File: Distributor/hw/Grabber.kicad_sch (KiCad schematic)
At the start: 13 parts, among them J1 Conn_01x04, J2 Conn_01x06_MountingPin, J3 Conn_02x09_Odd_Even, U2 STM32G070CBTx

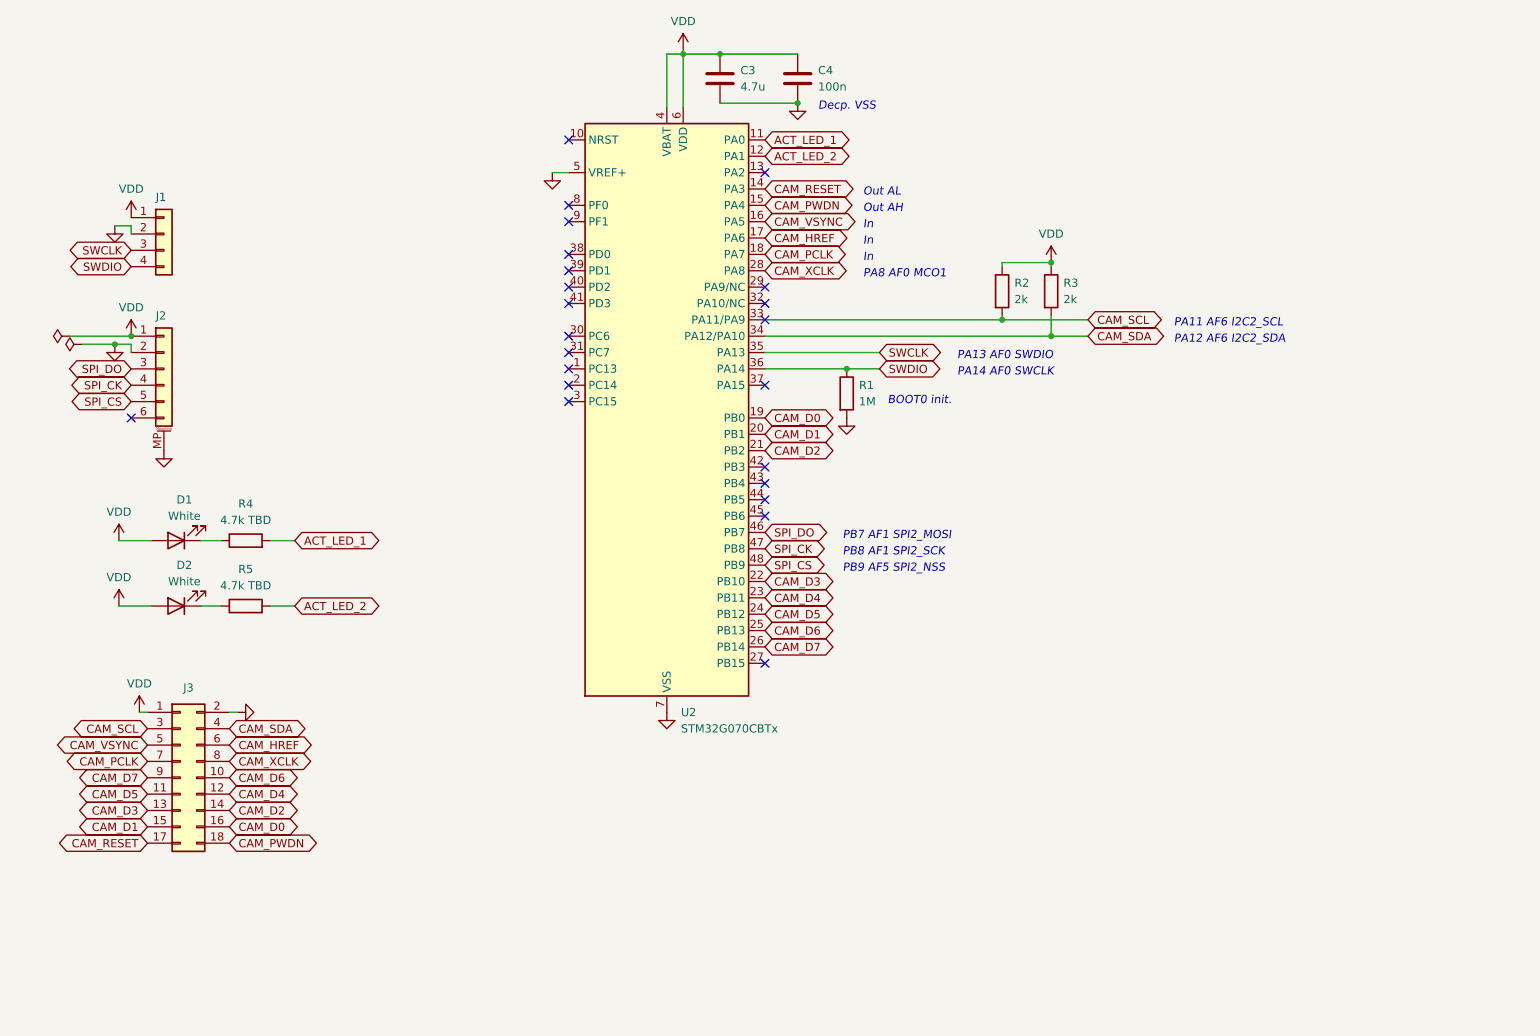
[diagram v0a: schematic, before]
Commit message: Merge distributor and grabber schematic into one
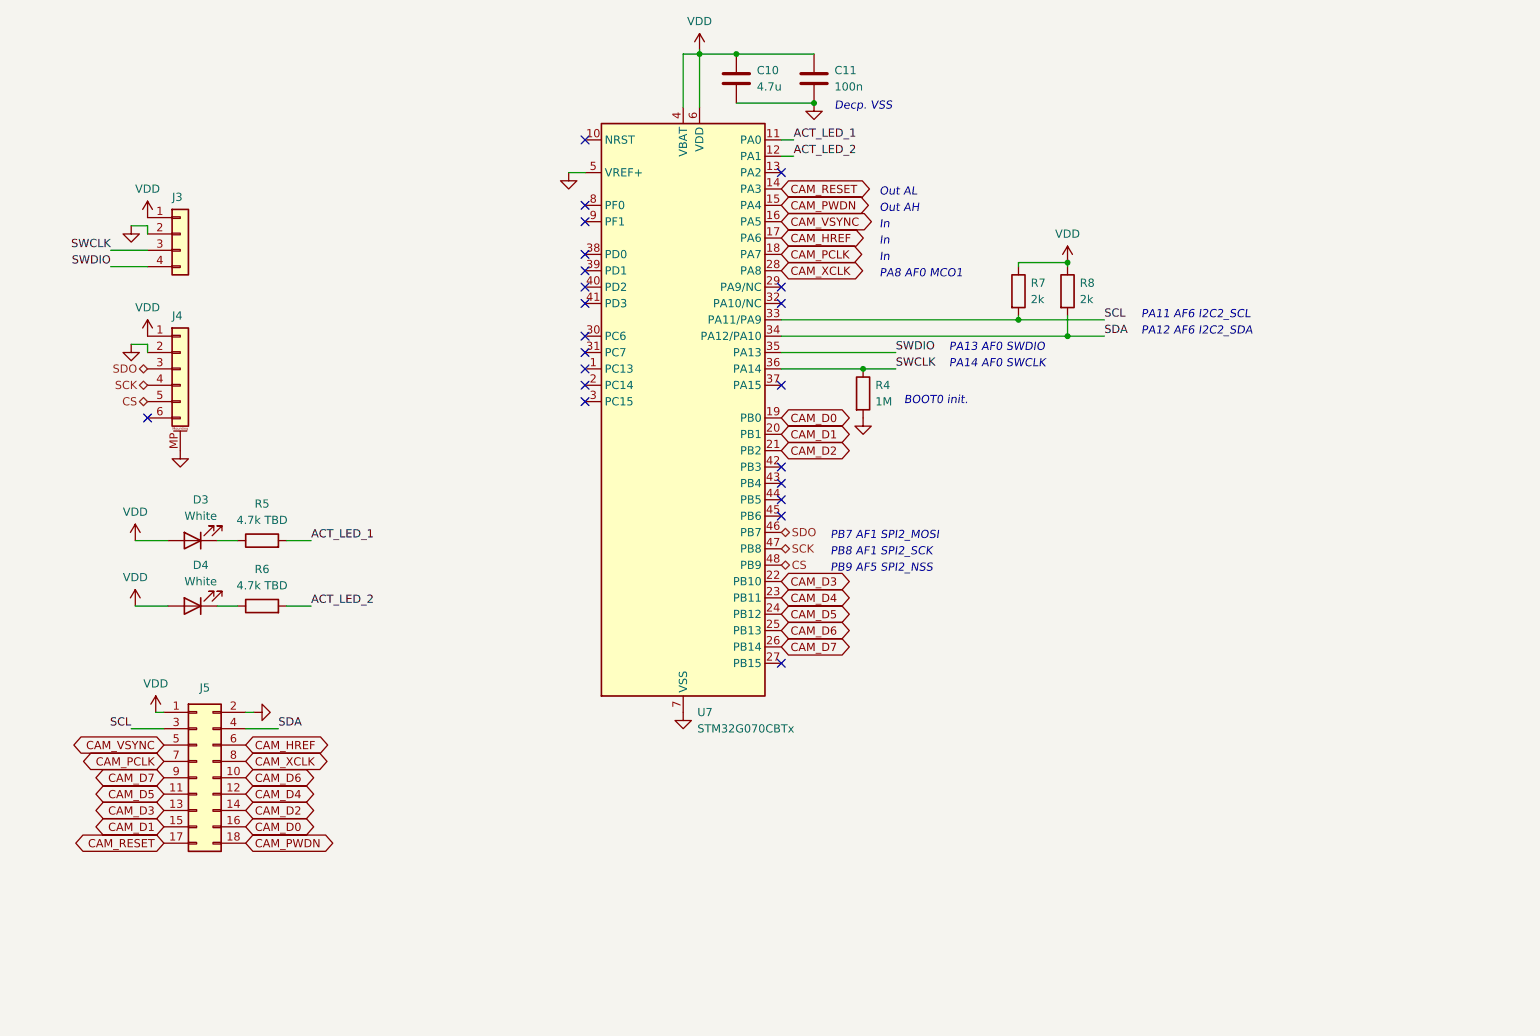
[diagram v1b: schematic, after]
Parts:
- removed C3: 4.7u, Capacitor_SMD:C_0603_1608Metric, symbol Device:C
- removed C4: 100n, Capacitor_SMD:C_0603_1608Metric, symbol Device:C
- removed D1, D2: White, LED_SMD:LED_0603_1608Metric, symbol Device:LED
- removed J1: Conn_01x04, Grabber_footprints:TestPoints_1x04_P2.0, symbol Connector_Generic:Conn_01x04
- removed J2: Conn_01x06_MountingPin, Connector_FFC-FPC:TE_84952-6_1x06-1MP_P1.0mm_Horizontal, symbol Connector_Generic_MountingPin:Conn_01x06_MountingPin
- removed J3: Conn_02x09_Odd_Even, Connector_PinHeader_2.54mm:PinHeader_2x09_P2.54mm_Vertical, symbol Connector_Generic:Conn_02x09_Odd_Even
- removed R1: 1M, Resistor_SMD:R_0603_1608Metric, symbol Device:R
- removed R2, R3: 2k, Resistor_SMD:R_0603_1608Metric, symbol Device:R
- removed U2: STM32G070CBTx, Package_QFP:LQFP-48_7x7mm_P0.5mm, symbol MCU_ST_STM32G0:STM32G070CBTx
- added C10: 4.7u, Capacitor_SMD:C_0603_1608Metric, symbol Device:C
- added C11: 100n, Capacitor_SMD:C_0603_1608Metric, symbol Device:C
- added D3, D4: White, LED_SMD:LED_0603_1608Metric, symbol Device:LED
- added J3: Conn_01x04, Distributor_footprints:TestPoints_1x04_P2.0, symbol Connector_Generic:Conn_01x04
- added J4: Conn_01x06_MountingPin, Connector_FFC-FPC:TE_84952-6_1x06-1MP_P1.0mm_Horizontal, symbol Connector_Generic_MountingPin:Conn_01x06_MountingPin
- added J5: Conn_02x09_Odd_Even, Connector_PinHeader_2.54mm:PinHeader_2x09_P2.54mm_Vertical, symbol Connector_Generic:Conn_02x09_Odd_Even
- added R6: 4.7k TBD, Resistor_SMD:R_0603_1608Metric, symbol Device:R
- added R7, R8: 2k, Resistor_SMD:R_0603_1608Metric, symbol Device:R
- added U7: STM32G070CBTx, Package_QFP:LQFP-48_7x7mm_P0.5mm, symbol MCU_ST_STM32G0:STM32G070CBTx
- R4: value 4.7k TBD -> 1M
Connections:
- net ACT_LED_1: now also R5.2, U7.11 (PA0); no longer R4.2
- net ACT_LED_2: now also R6.2, U7.12 (PA1); no longer R5.2
- net CAM_D0: now also J5.16 (Pin_16), U7.19 (PB0)
- net CAM_D1: now also J5.15 (Pin_15), U7.20 (PB1)
- net CAM_D2: now also J5.14 (Pin_14), U7.21 (PB2)
- net CAM_D3: now also J5.13 (Pin_13), U7.22 (PB10)
- net CAM_D4: now also J5.12 (Pin_12), U7.23 (PB11)
- net CAM_D5: now also J5.11 (Pin_11), U7.24 (PB12)
- net CAM_D6: now also J5.10 (Pin_10), U7.25 (PB13)
- net CAM_D7: now also J5.9 (Pin_9), U7.26 (PB14)
- net CAM_HREF: now also J5.6 (Pin_6), U7.17 (PA6)
- net CAM_PCLK: now also J5.7 (Pin_7), U7.18 (PA7)
- net CAM_PWDN: now also J5.18 (Pin_18), U7.15 (PA4)
- net CAM_RESET: now also J5.17 (Pin_17), U7.14 (PA3)
- net CAM_VSYNC: now also J5.5 (Pin_5), U7.16 (PA5)
- net CAM_XCLK: now also J5.8 (Pin_8), U7.28 (PA8)
- net GND: now also R4.2, C10.2, C11.2, J3.2 (Pin_2), J4.2 (Pin_2), J4.MP (MountPin), J5.2 (Pin_2), U7.5 (VREF+), U7.7 (VSS)
- net SWCLK: now also R4.1, J3.3 (Pin_3), U7.36 (PA14)
- net SWDIO: now also J3.4 (Pin_4), U7.35 (PA13)
- net VDD: now also C10.1, C11.1, D3.2 (A), D4.2 (A), J3.1 (Pin_1), J4.1 (Pin_1), J5.1 (Pin_1), R7.1, R8.1, U7.4 (VBAT), U7.6 (VDD)
- net at R5.1: now also D3.1 (K)
- new net: D4.1 (K), R6.1
- new net CS: J4.5 (Pin_5), U7.48 (PB9)
- new net SCK: J4.4 (Pin_4), U7.47 (PB8)
- new net SCL: J5.3 (Pin_3), R7.2, U7.33 (PA11/PA9)
- new net SDA: J5.4 (Pin_4), R8.2, U7.34 (PA12/PA10)
- new net SDO: J4.3 (Pin_3), U7.46 (PB7)
- no-connect marks 23 -> 22

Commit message: Add MLX90640 sensor to schematic
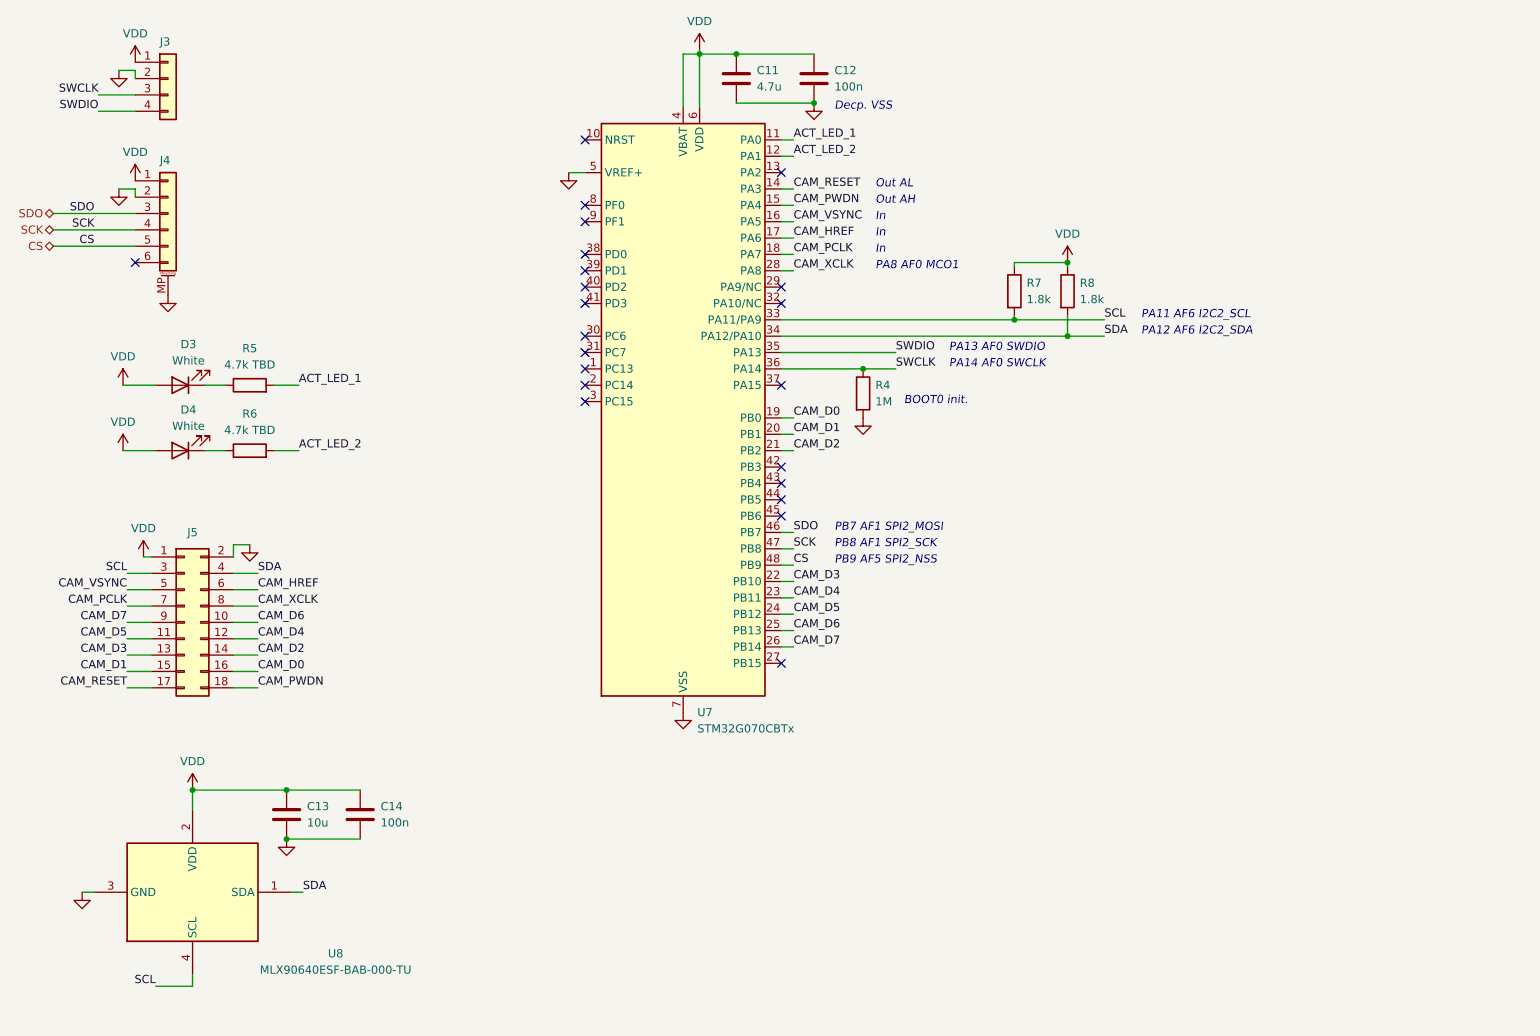
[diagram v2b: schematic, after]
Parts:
- added C13: 10u, Capacitor_SMD:C_0603_1608Metric, symbol Device:C
- added C14: 100n, Capacitor_SMD:C_0603_1608Metric, symbol Device:C
- added U8: MLX90640ESF-BAB-000-TU, MLX90640ESF-BAB-000-TU:MLX90640ESFBAB000TU, symbol MLX90640ESF-BAB-000-TU:MLX90640ESF-BAB-000-TU
- J4: footprint Connector_FFC-FPC:TE_84952-6_1x06-1MP_P1.0mm_Horizontal -> Connector_FFC-FPC:Jushuo_AFC07-S06FCA-00_1x6-1MP_P0.50_Horizontal
- R7, R8: value 2k -> 1.8k
- renumbered C10 to C11, C11 to C12
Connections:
- net GND: now also C13.2, C14.2, U8.3 (GND)
- net SCL: now also U8.4 (SCL)
- net SDA: now also U8.1 (SDA)
- net VDD: now also C13.1, C14.1, U8.2 (VDD)
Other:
- moved on the sheet: D3, D4, J3, J4, J5, R5, R6, R7

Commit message: Separate 5V power supplies into four domains
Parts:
- renumbered C11 to C13, C12 to C14, C13 to C15, C14 to C16, J3 to J7, J4 to J8, J5 to J9

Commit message: Board layout
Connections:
- net GND: no longer U7.5 (VREF+)
- net VDD: now also U7.5 (VREF+)
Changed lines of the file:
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@@
     (stroke (width 0) (type default))
   )
-  (wire (pts (xy 103.505 43.18) (xy 106.045 43.18))
+  (wire (pts (xy 102.235 43.18) (xy 106.045 43.18))
     (stroke (width 0) (type default))
   )
@@
         (path "/3f67d80a-1b5b-4b57-a63e-46eb7de4787a/d071538b-874a-4835-97d2-570c76260972"
           (reference "#PWR043") (unit 1)
-        )
-      )
-    )
-  )
-  (symbol (lib_id "power:GND") (at 103.505 43.18 0) (unit 1)
-    (in_bom yes) (on_board yes) (dnp no) (fields_autoplaced)
-    (property "Reference" "#PWR049" (at 103.505 49.53 0)
-      (effects (font (size 1.27 1.27)) hide)
-    )
-    (property "Value" "GND" (at 103.505 47.625 0)
-      (effects (font (size 1.27 1.27)) hide)
-    )
-    (property "Footprint" "" (at 103.505 43.18 0)
-      (effects (font (size 1.27 1.27)) hide)
-    )
-    (property "Datasheet" "" (at 103.505 43.18 0)
-      (effects (font (size 1.27 1.27)) hide)
-    )
-    (pin "1")
-    (instances
-      (project "Distributor"
-        (path "/3f67d80a-1b5b-4b57-a63e-46eb7de4787a/d071538b-874a-4835-97d2-570c76260972"
-          (reference "#PWR049") (unit 1)
         )
       )
@@
         )
       )
+    )
+  )
+  (symbol (lib_id "power:VDD") (at 102.235 43.18 0) (unit 1)
+    (in_bom yes) (on_board yes) (dnp no) (fields_autoplaced)
+    (property "Reference" "#PWR049" (at 102.235 46.99 0)
+      (effects (font (size 1.27 1.27)) hide)
+    )
+    (property "Value" "VDD" (at 102.235 38.735 0)
+      (effects (font (size 1.27 1.27)))
+    )
+    (property "Footprint" "" (at 102.235 43.18 0)
+      (effects (font (size 1.27 1.27)) hide)
+    )
+    (property "Datasheet" "" (at 102.235 43.18 0)
+      (effects (font (size 1.27 1.27)) hide)
+    )
+    (pin "1")
+    (instances
+      (project "Distributor"
+        (path "/3f67d80a-1b5b-4b57-a63e-46eb7de4787a/d071538b-874a-4835-97d2-570c76260972"
+          (reference "#PWR049") (unit 1)
+        )
+      )

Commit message: Finish routing
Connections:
- net CAM_HREF: now also U7.13 (PA2); no longer U7.17 (PA6)
- net CAM_PCLK: now also U7.27 (PB15); no longer U7.18 (PA7)
- net CAM_PWDN: now also U7.14 (PA3); no longer U7.15 (PA4)
- net CAM_RESET: now also U7.15 (PA4); no longer U7.14 (PA3)
- net CAM_VSYNC: now also U7.29 (PA9/NC); no longer U7.16 (PA5)
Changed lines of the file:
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@@
   (no_connect (at 106.045 63.5))
   (no_connect (at 136.525 63.5))
-  (no_connect (at 136.525 43.18))
-  (no_connect (at 136.525 119.38))
+  (no_connect (at 136.525 53.34))
   (no_connect (at 136.525 96.52))
   (no_connect (at 106.045 68.58))
   (no_connect (at 136.525 91.44))
-  (no_connect (at 136.525 60.96))
+  (no_connect (at 136.525 50.8))
   (no_connect (at 106.045 60.96))
+  (no_connect (at 136.525 55.88))
   (no_connect (at 106.045 38.1))
   (no_connect (at 106.045 71.12))
@@
     (stroke (width 0) (type default))
   )
-  (wire (pts (xy 138.43 50.8) (xy 136.525 50.8))
+  (wire (pts (xy 138.43 60.96) (xy 136.525 60.96))
     (stroke (width 0) (type default))
   )
@@
     (stroke (width 0) (type default))
   )
-  (wire (pts (xy 138.43 53.34) (xy 136.525 53.34))
+  (wire (pts (xy 138.43 43.18) (xy 136.525 43.18))
     (stroke (width 0) (type default))
   )
@@
     (stroke (width 0) (type default))
   )
-  (wire (pts (xy 138.43 55.88) (xy 136.525 55.88))
+  (wire (pts (xy 138.43 119.38) (xy 136.525 119.38))
     (stroke (width 0) (type default))
   )
@@
     (stroke (width 0) (type default))
   )
-  (text "In" (at 151.13 53.34 0)
-    (effects (font (size 1.27 1.27) italic) (justify left bottom))
-  )
-  (text "In" (at 151.13 55.88 0)
+  (text "In" (at 151.13 43.18 0)
+    (effects (font (size 1.27 1.27) italic) (justify left bottom))
+  )
+  (text "In" (at 151.13 119.38 0)
     (effects (font (size 1.27 1.27) italic) (justify left bottom))
   )
@@
     (effects (font (size 1.27 1.27) italic) (justify left bottom))
   )
-  (text "In" (at 151.13 50.8 0)
+  (text "In" (at 151.13 60.96 0)
     (effects (font (size 1.27 1.27) italic) (justify left bottom))
   )
@@
     (effects (font (size 1.27 1.27) italic) (justify left bottom))
   )
-  (text "Out AL" (at 151.13 45.72 0)
+  (text "Out AL" (at 151.13 48.26 0)
     (effects (font (size 1.27 1.27) italic) (justify left bottom))
   )
@@
     (effects (font (size 1.27 1.27) italic) (justify left bottom))
   )
-  (text "Out AH" (at 151.13 48.26 0)
+  (text "Out AH" (at 151.13 45.72 0)
     (effects (font (size 1.27 1.27) italic) (justify left bottom))
   )
@@
     (effects (font (size 1.27 1.27)) (justify right bottom))
   )
-  (label "CAM_RESET" (at 138.43 45.72 0) (fields_autoplaced)
+  (label "CAM_RESET" (at 138.43 48.26 0) (fields_autoplaced)
     (effects (font (size 1.27 1.27)) (justify left bottom))
   )
@@
     (effects (font (size 1.27 1.27)) (justify left bottom))
   )
-  (label "CAM_PWDN" (at 138.43 48.26 0) (fields_autoplaced)
+  (label "CAM_PWDN" (at 138.43 45.72 0) (fields_autoplaced)
     (effects (font (size 1.27 1.27)) (justify left bottom))
   )
@@
     (effects (font (size 1.27 1.27)) (justify right bottom))
   )
-  (label "CAM_PCLK" (at 138.43 55.88 0) (fields_autoplaced)
+  (label "CAM_PCLK" (at 138.43 119.38 0) (fields_autoplaced)
     (effects (font (size 1.27 1.27)) (justify left bottom))
   )
@@
     (effects (font (size 1.27 1.27)) (justify left bottom))
   )
-  (label "CAM_HREF" (at 138.43 53.34 0) (fields_autoplaced)
+  (label "CAM_HREF" (at 138.43 43.18 0) (fields_autoplaced)
     (effects (font (size 1.27 1.27)) (justify left bottom))
   )
@@
     (effects (font (size 1.27 1.27)) (justify right bottom))
   )
-  (label "CAM_VSYNC" (at 138.43 50.8 0) (fields_autoplaced)
-    (effects (font (size 1.27 1.27)) (justify left bottom))
-  )
+  (label "CAM_VSYNC" (at 138.43 60.96 0) (fields_autoplaced)
+    (effects (font (size 1.27 1.27)) (justify left bottom))
+  )
